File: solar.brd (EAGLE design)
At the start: 50 x 50 mm, 13 parts, among them J1 POWERPOLE_POWER10AWG, J2 POWERPOLE_POWER10AWG, J3 POWERPOLE_POWER10AWG, J4 POWERPOLE_POWER10AWG, J5 POWERPOLE_POWER10AWG

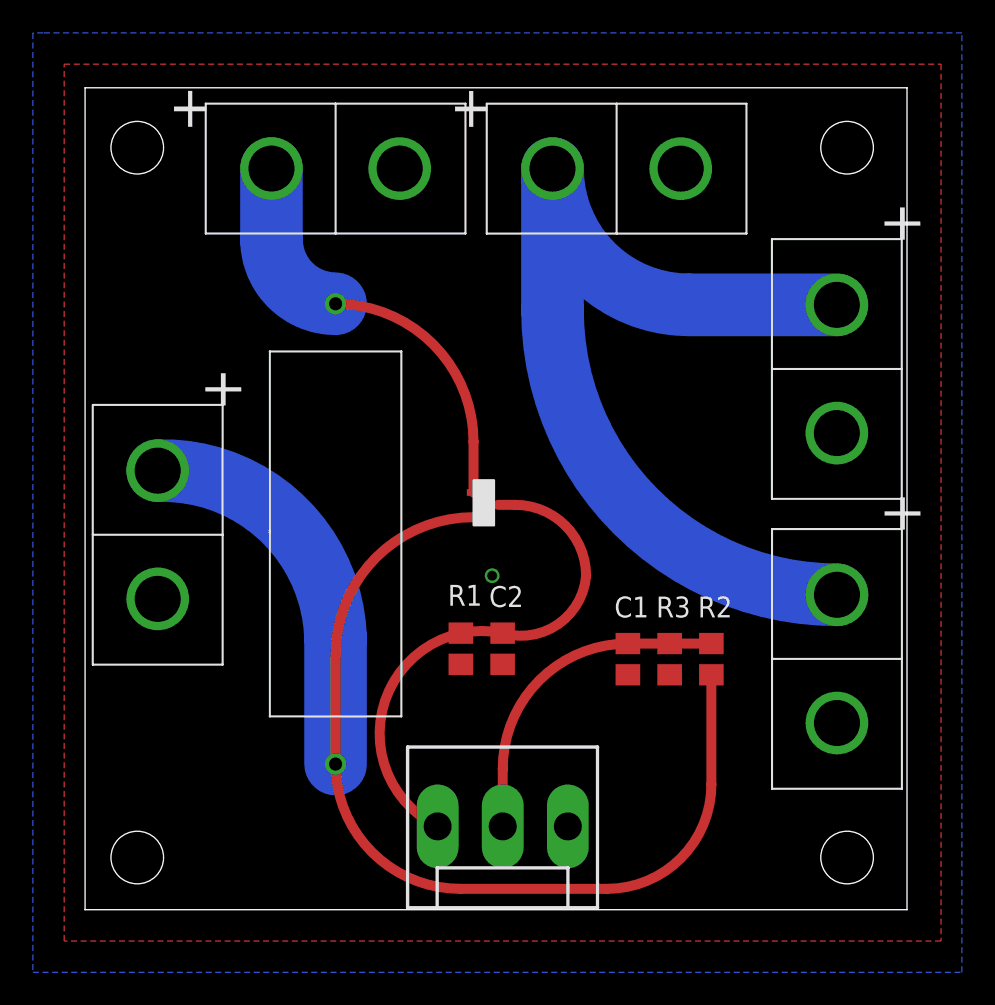
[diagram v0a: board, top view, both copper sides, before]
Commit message: Uses PCB mount instead of cable for power pole
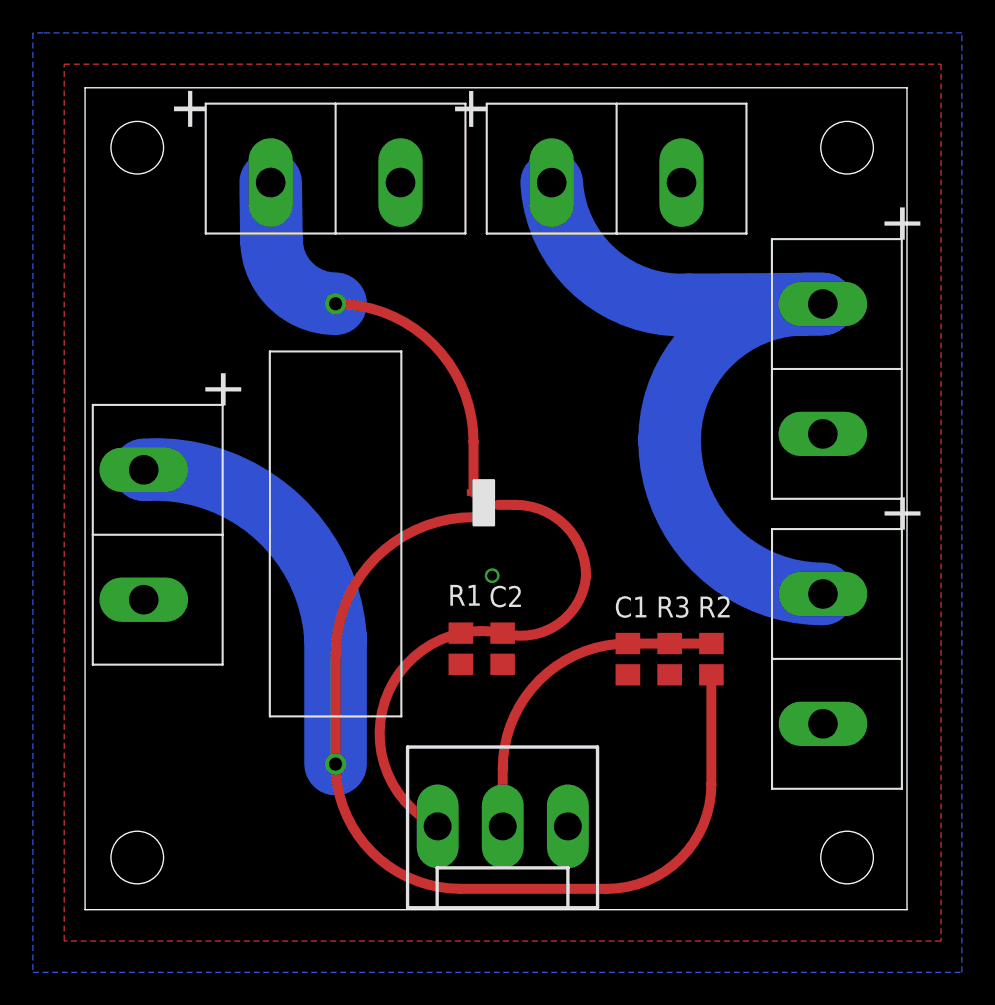
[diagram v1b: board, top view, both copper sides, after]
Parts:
- J1, J2, J3, J4, J5: value POWERPOLE_POWER10AWG -> POWERPOLE_POWER25A; device powerpoles:POWERPOLE_PAIR_10AWG -> powerpoles:POWERPOLE_PAIR_25A
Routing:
- net N$1: track 53.8 -> 45.3 mm
- net SOLAR_OUT: track 24.8 -> 23.9 mm
- net SOLAR_IN: track 76.3 -> 77.0 mm
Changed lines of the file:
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@@
 </autorouter>
 <elements>
-<element name="J1" library="powerpoles" package="POWERPOLE_PAIR_10AWG" value="POWERPOLE_POWER10AWG" x="4.4196" y="22.8092" smashed="yes" rot="R270"/>
-<element name="J2" library="powerpoles" package="POWERPOLE_PAIR_10AWG" value="POWERPOLE_POWER10AWG" x="45.7392" y="15.2576" rot="R270"/>
-<element name="J3" library="powerpoles" package="POWERPOLE_PAIR_10AWG" value="POWERPOLE_POWER10AWG" x="15.24" y="45.085"/>
-<element name="J4" library="powerpoles" package="POWERPOLE_PAIR_10AWG" value="POWERPOLE_POWER10AWG" x="45.7322" y="32.8948" rot="R270"/>
-<element name="J5" library="powerpoles" package="POWERPOLE_PAIR_10AWG" value="POWERPOLE_POWER10AWG" x="32.3346" y="45.0812"/>
+<element name="J1" library="powerpoles" package="POWERPOLE_PAIR_25A" value="POWERPOLE_POWER25A" x="4.4196" y="22.8092" smashed="yes" rot="R270"/>
+<element name="J2" library="powerpoles" package="POWERPOLE_PAIR_25A" value="POWERPOLE_POWER25A" x="45.7392" y="15.2576" rot="R270"/>
+<element name="J3" library="powerpoles" package="POWERPOLE_PAIR_25A" value="POWERPOLE_POWER25A" x="15.24" y="45.085"/>
+<element name="J4" library="powerpoles" package="POWERPOLE_PAIR_25A" value="POWERPOLE_POWER25A" x="45.7322" y="32.8948" rot="R270"/>
+<element name="J5" library="powerpoles" package="POWERPOLE_PAIR_25A" value="POWERPOLE_POWER25A" x="32.3346" y="45.0812"/>
 <element name="U$1" library="power" package="ER58R03KT" value="ER58R03KT" x="15.24" y="22.86" smashed="yes" rot="R90"/>
 <element name="U$2" library="power" package="ZXCT1009-SOT" value="ZXCT1009" x="24.13" y="24.13" rot="R180"/>
@@
 <contactref element="J4" pad="RED"/>
 <contactref element="J5" pad="RED"/>
-<wire x1="45.7322" y1="36.7948" x2="36.721" y2="36.7948" width="3.81" layer="16"/>
-<wire x1="36.721" y1="36.7948" x2="28.4346" y2="45.0812" width="3.81" layer="16" curve="-90"/>
-<wire x1="45.7392" y1="19.1576" x2="28.4346" y2="36.4622" width="3.81" layer="16" curve="-90"/>
-<wire x1="28.4346" y1="36.4622" x2="28.4346" y2="45.0812" width="3.81" layer="16"/>
+<wire x1="44.8822" y1="36.8448" x2="36.721" y2="36.7948" width="3.81" layer="16"/>
+<wire x1="36.721" y1="36.7948" x2="28.3846" y2="44.2312" width="3.81" layer="16" curve="-90"/>
+<wire x1="44.8822" y1="36.8448" x2="43.8298" y2="36.8448" width="3.81" layer="16"/>
+<wire x1="43.8298" y1="36.8448" x2="35.56" y2="28.575" width="3.81" layer="16" curve="90"/>
+<wire x1="35.56" y1="28.575" x2="35.56" y2="28.5368" width="3.81" layer="16"/>
+<wire x1="35.56" y1="28.5368" x2="44.8892" y2="19.2076" width="3.81" layer="16" curve="90"/>
 </signal>
 <signal name="SOLAR_IN">
@@
 <contactref element="U$2" pad="P$2"/>
 <contactref element="R2" pad="2"/>
-<wire x1="4.4196" y1="26.7092" x2="15.24" y2="16.5238" width="3.81" layer="16" curve="-90"/>
+<wire x1="3.5696" y1="26.7592" x2="15.24" y2="16.5238" width="3.81" layer="16" curve="-90"/>
 <wire x1="15.24" y1="16.5238" x2="15.24" y2="8.86" width="3.81" layer="16"/>
 <wire x1="23.63" y1="23.88" x2="15.24" y2="15.49" width="0.6096" layer="1" curve="90"/>
@@
 <wire x1="23.63" y1="28.47" x2="23.63" y2="25.38" width="0.6096" layer="1"/>
 <wire x1="15.24" y1="36.86" x2="11.34" y2="40.76" width="3.81" layer="16" curve="-90"/>
-<wire x1="11.34" y1="40.76" x2="11.34" y2="45.085" width="3.81" layer="16"/>
+<wire x1="11.34" y1="40.76" x2="11.29" y2="44.235" width="3.81" layer="16"/>
 </signal>
 <signal name="CURR_OUT">
